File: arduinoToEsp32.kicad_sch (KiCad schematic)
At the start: 0 parts

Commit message: adicionado os componentes
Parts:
- added J1: Conn_01x03_Pin, Connector_Wire:SolderWire-0.75sqmm_1x03_P4.8mm_D1.25mm_OD2.3mm, symbol Connector:Conn_01x03_Pin
- added R1: R, Resistor_THT:R_Axial_DIN0309_L9.0mm_D3.2mm_P15.24mm_Horizontal, symbol Device:R

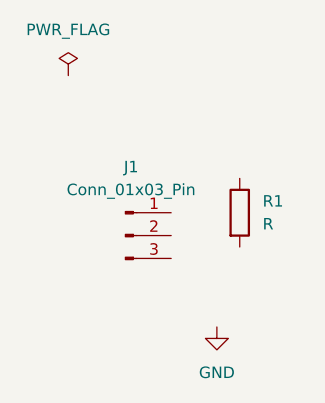
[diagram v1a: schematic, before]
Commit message: adicionado os componentes ligações
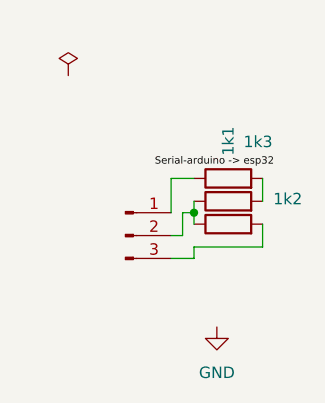
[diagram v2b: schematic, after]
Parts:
- added 1k2, 1k3: R, Resistor_THT:R_Axial_DIN0309_L9.0mm_D3.2mm_P15.24mm_Horizontal, symbol Device:R
- renumbered R1 to 1k1
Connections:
- net at J1.1 (Pin_1): now also 1k1.1
- net at J1.2 (Pin_2): now also 1k2.1, 1k3.1
- net at J1.3 (Pin_3): now also 1k3.2
- net at 1k1.2: now also 1k2.2
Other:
- moved on the sheet: 1k1

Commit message: esquematico instalado
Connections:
- net GND: now also 1k3.2, J1.3 (Pin_3)
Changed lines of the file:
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@@
 	(paper "A4")
+	(junction
+		(at 93.98 74.93)
+		(diameter 0)
+		(color 0 0 0 0)
+	)
 	(junction
 		(at 91.44 71.12)
@@
 		(color 0 0 0 0)
 	)
-	(wire
-		(pts
-			(xy 99.06 74.93) (xy 91.44 74.93)
+	(junction
+		(at 88.9 67.31)
+		(diameter 0)
+		(color 0 0 0 0)
+	)
+	(wire
+		(pts
+			(xy 99.06 74.93) (xy 93.98 74.93)
 		)
 		(stroke
@@
 	(wire
 		(pts
+			(xy 86.36 60.96) (xy 88.9 60.96)
+		)
+		(stroke
+			(width 0)
+			(type default)
+		)
+	)
+	(wire
+		(pts
 			(xy 90.17 73.66) (xy 90.17 71.12)
+		)
+		(stroke
+			(width 0)
+			(type default)
+		)
+	)
+	(wire
+		(pts
+			(xy 88.9 60.96) (xy 88.9 67.31)
+		)
+		(stroke
+			(width 0)
+			(type default)
+		)
+	)
+	(wire
+		(pts
+			(xy 93.98 74.93) (xy 91.44 74.93)
 		)
 		(stroke
@@
 	(symbol
 		(lib_id "power:GND")
-		(at 93.98 83.82 0)
+		(at 93.98 74.93 0)
 		(unit 1)
 		(exclude_from_sim no)
@@
 		(fields_autoplaced yes)
 		(property "Reference" "#PWR01"
-			(at 93.98 90.17 0)
+			(at 93.98 81.28 0)
 			(effects
 				(font
@@
 		)
 		(property "Value" "GND"
-			(at 93.98 88.9 0)
+			(at 93.98 80.01 0)
 			(effects
 				(font
@@
 		)
 		(property "Footprint" ""
-			(at 93.98 83.82 0)
+			(at 93.98 74.93 0)
 			(effects
 				(font
@@
 		)
 		(property "Datasheet" ""
-			(at 93.98 83.82 0)
+			(at 93.98 74.93 0)
 			(effects
 				(font
@@
 		)
 		(property "Description" "Power symbol creates a global label with name \"GND\" , ground"
-			(at 93.98 83.82 0)
+			(at 93.98 74.93 0)
 			(effects
 				(font
@@
 	(symbol
 		(lib_id "power:PWR_FLAG")
-		(at 77.47 55.88 0)
+		(at 86.36 60.96 0)
 		(unit 1)
 		(exclude_from_sim no)
@@
 		(fields_autoplaced yes)
 		(property "Reference" "#FLG01"
-			(at 77.47 53.975 0)
+			(at 86.36 59.055 0)
 			(effects
 				(font
@@
 		)
 		(property "Value" "PWR_FLAG"
-			(at 77.47 50.8 0)
+			(at 86.36 55.88 0)
 			(effects
 				(font
@@
 		)
 		(property "Footprint" ""
-			(at 77.47 55.88 0)
+			(at 86.36 60.96 0)
 			(effects
 				(font
@@
 		)
 		(property "Datasheet" "~"
-			(at 77.47 55.88 0)
+			(at 86.36 60.96 0)
 			(effects
 				(font
@@
 		)
 		(property "Description" "Special symbol for telling ERC where power comes from"
-			(at 77.47 55.88 0)
-			(effects
-				(font
+			(at 86.36 60.96 0)
+			(effects
+				(font

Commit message: correção do esquematico
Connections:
- net +5V: now reaches 1k1.1, J1.1 (Pin_1)
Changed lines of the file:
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@@
 	(paper "A4")
-	(junction
-		(at 93.98 74.93)
-		(diameter 0)
-		(color 0 0 0 0)
-	)
 	(junction
 		(at 91.44 71.12)
@@
 		(color 0 0 0 0)
 	)
-	(wire
-		(pts
-			(xy 99.06 74.93) (xy 93.98 74.93)
-		)
-		(stroke
-			(width 0)
-			(type default)
-		)
+	(junction
+		(at 88.9 78.74)
+		(diameter 0)
+		(color 0 0 0 0)
+	)
+	(junction
+		(at 88.9 76.2)
+		(diameter 0)
+		(color 0 0 0 0)
 	)
 	(wire
@@
 	(wire
 		(pts
+			(xy 87.63 67.31) (xy 88.9 67.31)
+		)
+		(stroke
+			(width 0)
+			(type default)
+		)
+	)
+	(wire
+		(pts
 			(xy 86.36 60.96) (xy 88.9 60.96)
 		)
@@
 	(wire
 		(pts
-			(xy 93.98 74.93) (xy 91.44 74.93)
+			(xy 88.9 78.74) (xy 88.9 76.2)
+		)
+		(stroke
+			(width 0)
+			(type default)
+		)
+	)
+	(wire
+		(pts
+			(xy 91.44 74.93) (xy 99.06 74.93)
 		)
 		(stroke
@@
 		)
 	)
-	(label "Serial-arduino -> esp32"
-		(at 100.33 66.04 180)
-		(effects
-			(font
-				(size 0.8128 0.8128)
-			)
-			(justify right bottom)
+	(wire
+		(pts
+			(xy 87.63 78.74) (xy 88.9 78.74)
+		)
+		(stroke
+			(width 0)
+			(type default)
+		)
+	)
+	(wire
+		(pts
+			(xy 92.71 78.74) (xy 88.9 78.74)
+		)
+		(stroke
+			(width 0)
+			(type default)
 		)
 	)
@@
 	(symbol
 		(lib_id "power:GND")
-		(at 93.98 74.93 0)
+		(at 87.63 78.74 0)
 		(unit 1)
 		(exclude_from_sim no)
@@
 		(fields_autoplaced yes)
 		(property "Reference" "#PWR01"
-			(at 93.98 81.28 0)
+			(at 87.63 85.09 0)
 			(effects
 				(font
@@
 		)
 		(property "Value" "GND"
-			(at 93.98 80.01 0)
+			(at 87.63 83.82 0)
 			(effects
 				(font
@@
 		)
 		(property "Footprint" ""
-			(at 93.98 74.93 0)
+			(at 87.63 78.74 0)
 			(effects
 				(font
@@
 		)
 		(property "Datasheet" ""
-			(at 93.98 74.93 0)
+			(at 87.63 78.74 0)
 			(effects
 				(font
@@
 		)
 		(property "Description" "Power symbol creates a global label with name \"GND\" , ground"
-			(at 93.98 74.93 0)
+			(at 87.63 78.74 0)
 			(effects
 				(font
@@
 				(path "/1b30a8e2-a201-4aed-8eb4-6b771745c9eb"
 					(reference "#PWR01")
+					(unit 1)
+				)
+			)
+		)
+	)
+	(symbol
+		(lib_id "power:+5V")
+		(at 87.63 67.31 90)
+		(unit 1)
+		(exclude_from_sim no)
+		(in_bom yes)
+		(on_board yes)
+		(dnp no)
+		(fields_autoplaced yes)
+		(property "Reference" "#PWR02"
+			(at 91.44 67.31 0)
+			(effects
+				(font
+					(size 1.27 1.27)
+				)
+				(hide yes)
+			)
+		)
+		(property "Value" "+5V"
+			(at 83.82 67.3099 90)
+			(effects
+				(font
+					(size 1.27 1.27)
+				)
+				(justify left)
+			)
+		)
+		(property "Footprint" ""
+			(at 87.63 67.31 0)
+			(effects
+				(font
+					(size 1.27 1.27)
+				)
+				(hide yes)
+			)
+		)
+		(property "Datasheet" ""
+			(at 87.63 67.31 0)
+			(effects
+				(font
+					(size 1.27 1.27)
+				)
+				(hide yes)
+			)
+		)
+		(property "Description" "Power symbol creates a global label with name \"+5V\""
+			(at 87.63 67.31 0)
+			(effects
+				(font
+					(size 1.27 1.27)
+				)
+				(hide yes)
+			)
+		)
+		(pin "1"
+		)
+		(instances
+			(project ""
+				(path "/1b30a8e2-a201-4aed-8eb4-6b771745c9eb"
+					(reference "#PWR02")
 					(unit 1)
 				)
@@
 					(unit 1)
 				)
+			)
+		)
+	)
+	(symbol
+		(lib_id "power:PWR_FLAG")
+		(at 92.71 78.74 270)
+		(unit 1)
+		(exclude_from_sim no)
+		(in_bom yes)
+		(on_board yes)
+		(dnp no)
+		(fields_autoplaced yes)
+		(property "Reference" "#FLG02"
+			(at 94.615 78.74 0)
+			(effects
+				(font
+					(size 1.27 1.27)
+				)
+				(hide yes)
+			)
+		)
+		(property "Value" "PWR_FLAG"
+			(at 97.79 78.74 0)
+			(effects
+				(font
+					(size 1.27 1.27)
+				)
+				(hide yes)
+			)
+		)
+		(property "Footprint" ""
+			(at 92.71 78.74 0)
+			(effects
+				(font
+					(size 1.27 1.27)
+				)
+				(hide yes)
+			)
+		)
+		(property "Datasheet" "~"
+			(at 92.71 78.74 0)
+			(effects
+				(font
+					(size 1.27 1.27)
+				)
+				(hide yes)
+			)
+		)
+		(property "Description" "Special symbol for telling ERC where power comes from"
+			(at 92.71 78.74 0)
+			(effects
+				(font
+					(size 1.27 1.27)
+				)
+				(hide yes)
+			)
+		)
+		(pin "1"
+		)
+		(instances
+			(project "arduinoToEsp32"
+				(path "/1b30a8e2-a201-4aed-8eb4-6b771745c9eb"
+					(reference "#FLG02")
+					(unit 1)
+				)
